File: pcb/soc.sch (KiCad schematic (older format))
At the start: 21 parts, among them IC5 CC2541F128RHAT, J1 CC Debugger, SW1 SW_Push, Y1 32 Mhz

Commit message: Added some documentation + TODO's
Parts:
- added C?: 1μF, symbol C_Small
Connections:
- net Earth: now also IC5.41 (GND(2)), C?.1
- net PIR_HIGH: now also IC5.9 (P1_1)
- net PIR_LOW: now also IC5.11 (P1_0)
- net at IC5.40 (DCOUPL): now also C?.2
- no-connect marks 2 -> 10
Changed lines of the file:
@@
 Comment4 ""
 $EndDescr
-Text HLabel 1200 4200 0    60   Input ~ 0
+Text HLabel 4050 3900 0    60   Input ~ 0
 PIR_HIGH
-Text HLabel 1200 4500 0    60   Input ~ 0
+Text HLabel 4500 4900 0    60   Input ~ 0
 PIR_LOW
 $Comp
@@
 L VCC #PWR22
 U 1 1 5A76E05D
-P 3850 3950
-F 0 "#PWR22" H 3850 3800 50  0001 C CNN
-F 1 "VCC" H 3850 4100 50  0000 C CNN
-F 2 "" H 3850 3950 50  0001 C CNN
-F 3 "" H 3850 3950 50  0001 C CNN
-	1    3850 3950
+P 3850 4250
+F 0 "#PWR22" H 3850 4100 50  0001 C CNN
+F 1 "VCC" H 3850 4400 50  0000 C CNN
+F 2 "" H 3850 4250 50  0001 C CNN
+F 3 "" H 3850 4250 50  0001 C CNN
+	1    3850 4250
 	1    0    0    -1
 $EndComp
@@
 Connection ~ 5950 3700
 Wire Wire Line
-	4250 4000 3850 4000
-Wire Wire Line
-	3850 4000 3850 3950
+	4250 4000 4100 4000
+Wire Wire Line
+	4100 4000 4100 4300
+Wire Wire Line
+	4100 4300 3850 4300
+Wire Wire Line
+	3850 4300 3850 4250
 Wire Wire Line
 	5550 1900 5550 1750
@@
 	1050 2550 1050 2400
 Wire Wire Line
-	1050 2000 1050 1850
+	1050 1850 1050 2000
 Wire Wire Line
 	1050 1550 1050 1400
@@
 Text Notes 2700 6300 2    60   ~ 0
 Debugger interface
+NoConn ~ 5350 4800
+NoConn ~ 5250 4800
+NoConn ~ 5150 4800
+NoConn ~ 5050 4800
+NoConn ~ 4950 4800
+NoConn ~ 4850 4800
+NoConn ~ 4750 4800
+NoConn ~ 4650 4800
+$Comp
+L Earth #PWR?
+U 1 1 5A76FB36
+P 4250 1900
+F 0 "#PWR?" H 4250 1650 50  0001 C CNN
+F 1 "Earth" H 4250 1750 50  0001 C CNN
+F 2 "" H 4250 1900 50  0001 C CNN
+F 3 "" H 4250 1900 50  0001 C CNN
+	1    4250 1900
+	1    0    0    -1
+$EndComp
+Wire Wire Line
+	4550 1900 4550 1800
+Wire Wire Line
+	4550 1800 4250 1800
+Wire Wire Line
+	4250 1800 4250 1900
+$Comp
+L C_Small C?
+U 1 1 5A770125
+P 4000 1650
+F 0 "C?" H 4010 1720 50  0000 L CNN
+F 1 "1μF" H 4010 1570 50  0000 L CNN
+F 2 "" H 4000 1650 50  0001 C CNN
+F 3 "" H 4000 1650 50  0001 C CNN
+	1    4000 1650
+	-1   0    0    1
+$EndComp
+$Comp
+L Earth #PWR?
+U 1 1 5A7703A1
+P 4000 1900
+F 0 "#PWR?" H 4000 1650 50  0001 C CNN
+F 1 "Earth" H 4000 1750 50  0001 C CNN
+F 2 "" H 4000 1900 50  0001 C CNN
+F 3 "" H 4000 1900 50  0001 C CNN
+	1    4000 1900
+	1    0    0    -1
+$EndComp
+Wire Wire Line
+	4650 1900 4650 1450
+Wire Wire Line
+	4000 1450 4000 1550
+Wire Wire Line
+	4000 1750 4000 1900
+Wire Wire Line
+	4650 1450 4000 1450
+Wire Wire Line
+	4250 3900 4050 3900
+Wire Wire Line
+	4500 4900 4550 4900
+Wire Wire Line
+	4550 4900 4550 4800
 $EndSCHEMATC

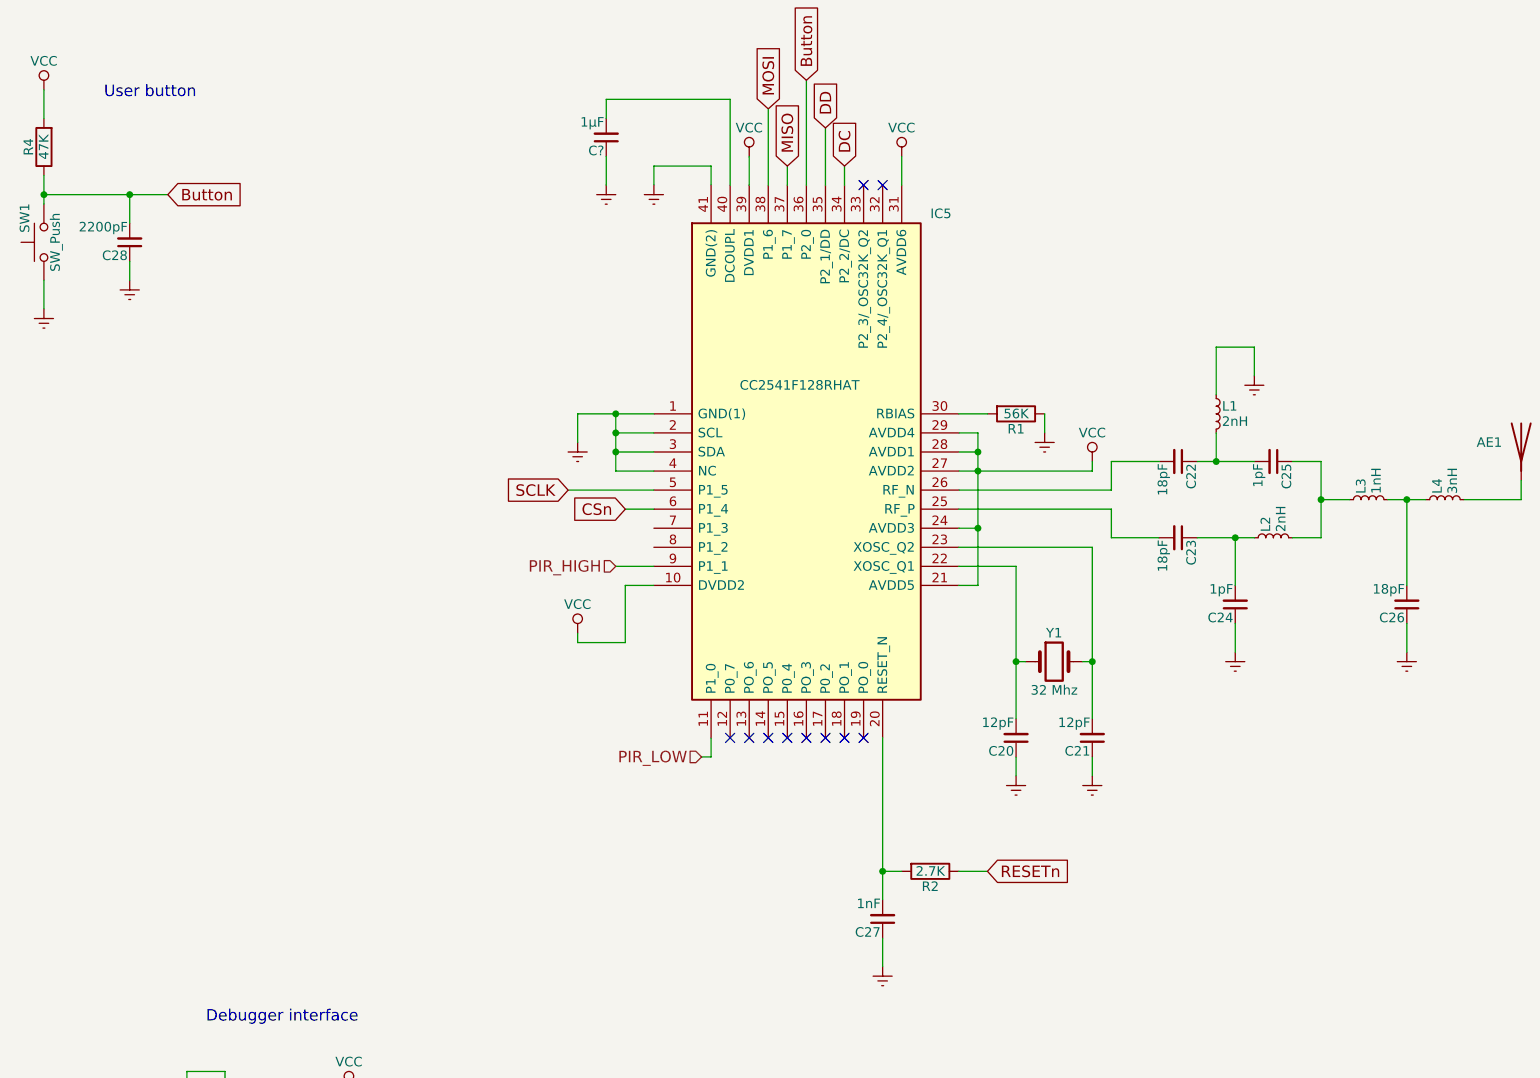
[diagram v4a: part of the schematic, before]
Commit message: Added light sensor with IIC interface
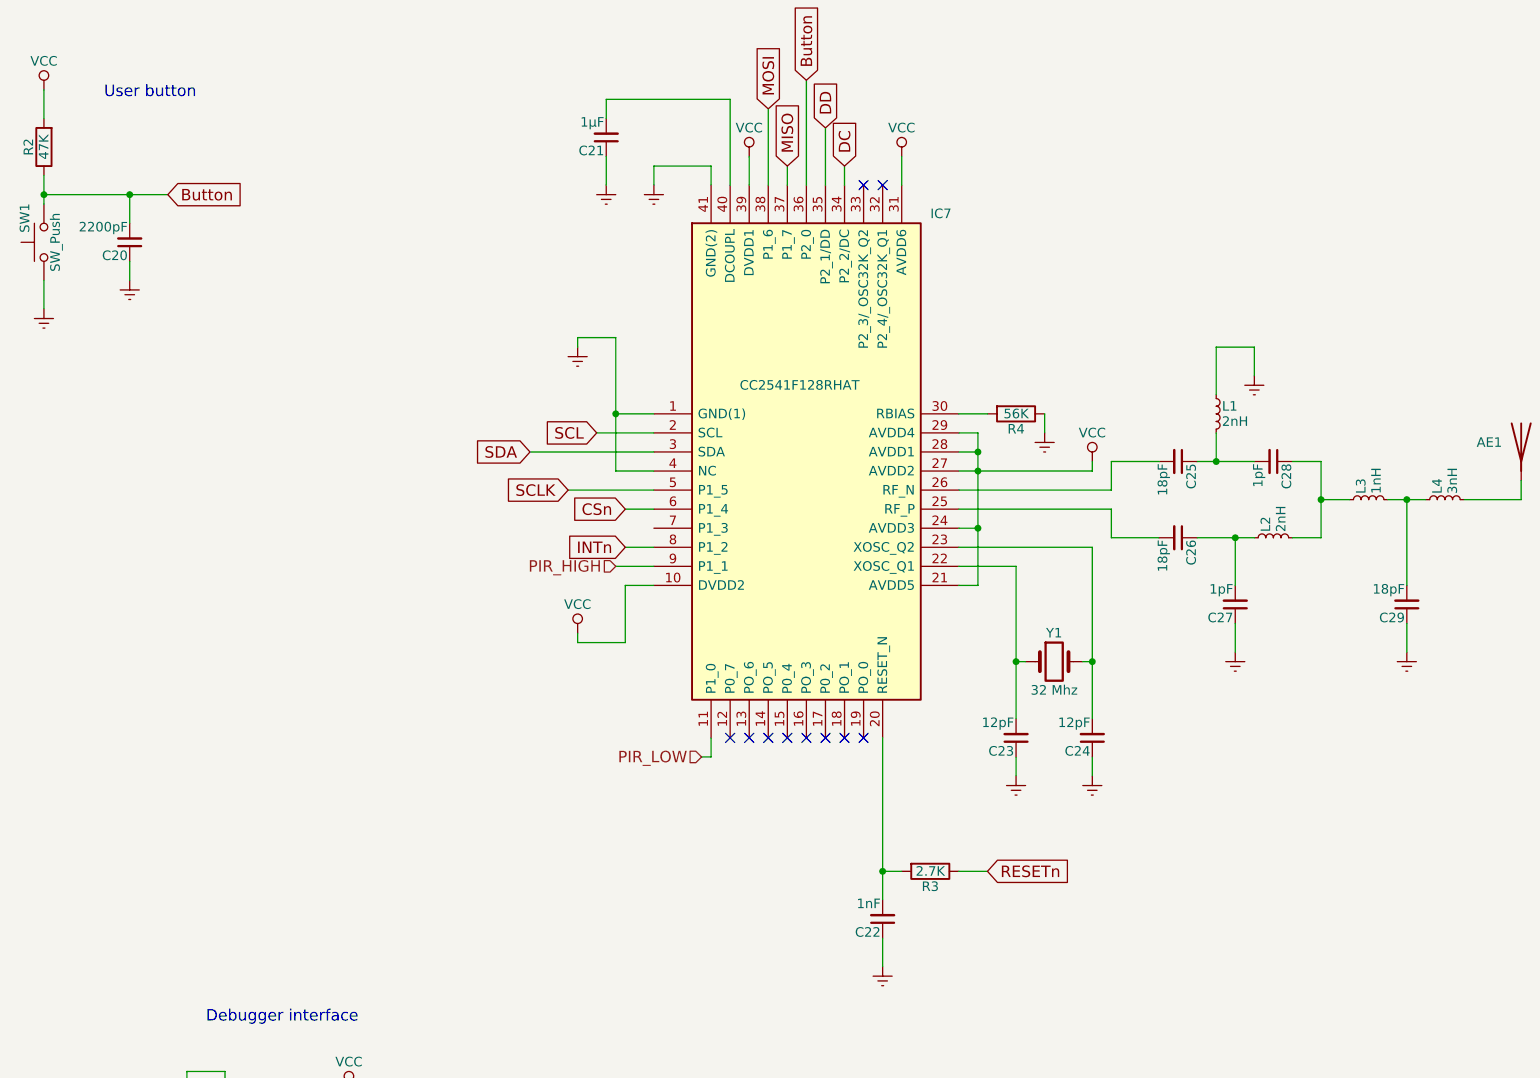
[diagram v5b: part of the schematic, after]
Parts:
- gave numbers to parts that had none: 1
- renumbered C28 to C20, C27 to C22, C20 to C23, C21 to C24, C22 to C25, C23 to C26, C24 to C27, C25 to C28, C26 to C29, IC5 to IC7, R4 to R2, R2 to R3, R1 to R4
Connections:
- net Earth: no longer IC7.2 (SCL), IC7.3 (SDA)
- net INTn: now reaches IC7.8 (P1_2)
- new net SCL: IC7.2 (SCL)
- new net SDA: IC7.3 (SDA)
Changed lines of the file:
@@
 LIBS:CC2541F256RHAR
 LIBS:CC2541F128RHAT
+LIBS:MAX44009EDT+T
 LIBS:pir-cache
 EELAYER 25 0
@@
 PIR_LOW
 $Comp
-L CC2541F128RHAT IC5
+L CC2541F128RHAT IC7
 U 1 1 5A76B408
 P 4250 3100
-F 0 "IC5" H 5700 4150 50  0000 L CNN
+F 0 "IC7" H 5700 4150 50  0000 L CNN
 F 1 "CC2541F128RHAT" H 4700 3250 50  0000 L CNN
 F 2 "QFN50P600X600X100-41N" H 5700 1450 50  0001 L CNN
@@
 SHUTTER
 $Comp
-L Earth #PWR21
+L Earth #PWR24
 U 1 1 5A76DE63
-P 3850 3250
-F 0 "#PWR21" H 3850 3000 50  0001 C CNN
-F 1 "Earth" H 3850 3100 50  0001 C CNN
-F 2 "" H 3850 3250 50  0001 C CNN
-F 3 "" H 3850 3250 50  0001 C CNN
-	1    3850 3250
-	1    0    0    -1
-$EndComp
-$Comp
-L VCC #PWR28
+P 3850 2750
+F 0 "#PWR24" H 3850 2500 50  0001 C CNN
+F 1 "Earth" H 3850 2600 50  0001 C CNN
+F 2 "" H 3850 2750 50  0001 C CNN
+F 3 "" H 3850 2750 50  0001 C CNN
+	1    3850 2750
+	1    0    0    -1
+$EndComp
+$Comp
+L VCC #PWR33
 U 1 1 5A76DE98
 P 6550 3350
-F 0 "#PWR28" H 6550 3200 50  0001 C CNN
+F 0 "#PWR33" H 6550 3200 50  0001 C CNN
 F 1 "VCC" H 6550 3500 50  0000 C CNN
 F 2 "" H 6550 3350 50  0001 C CNN
@@
 $EndComp
 $Comp
-L VCC #PWR22
+L VCC #PWR25
 U 1 1 5A76E05D
 P 3850 4250
-F 0 "#PWR22" H 3850 4100 50  0001 C CNN
+F 0 "#PWR25" H 3850 4100 50  0001 C CNN
 F 1 "VCC" H 3850 4400 50  0000 C CNN
 F 2 "" H 3850 4250 50  0001 C CNN
@@
 $EndComp
 $Comp
-L VCC #PWR25
+L VCC #PWR30
 U 1 1 5A76E1D1
 P 5550 1750
-F 0 "#PWR25" H 5550 1600 50  0001 C CNN
+F 0 "#PWR30" H 5550 1600 50  0001 C CNN
 F 1 "VCC" H 5550 1900 50  0000 C CNN
 F 2 "" H 5550 1750 50  0001 C CNN
@@
 $EndComp
 $Comp
-L VCC #PWR23
+L VCC #PWR28
 U 1 1 5A76E1F7
 P 4750 1750
-F 0 "#PWR23" H 4750 1600 50  0001 C CNN
+F 0 "#PWR28" H 4750 1600 50  0001 C CNN
 F 1 "VCC" H 4750 1900 50  0000 C CNN
 F 2 "" H 4750 1750 50  0001 C CNN
@@
 NoConn ~ 5350 1900
 $Comp
-L R R1
+L R R4
 U 1 1 5A76E4F0
 P 6150 3100
-F 0 "R1" V 6230 3100 50  0000 C CNN
+F 0 "R4" V 6230 3100 50  0000 C CNN
 F 1 "56K" V 6150 3100 50  0000 C CNN
 F 2 "" V 6080 3100 50  0001 C CNN
@@
 $EndComp
 $Comp
-L C_Small C22
+L C_Small C25
 U 1 1 5A76E83A
 P 7000 3350
-F 0 "C22" H 7010 3420 50  0000 L CNN
+F 0 "C25" H 7010 3420 50  0000 L CNN
 F 1 "18pF" H 7010 3270 50  0000 L CNN
 F 2 "" H 7000 3350 50  0001 C CNN
@@
 $EndComp
 $Comp
-L C_Small C23
+L C_Small C26
 U 1 1 5A76EB9B
 P 7000 3750
-F 0 "C23" H 7010 3820 50  0000 L CNN
+F 0 "C26" H 7010 3820 50  0000 L CNN
 F 1 "18pF" H 7010 3670 50  0000 L CNN
 F 2 "" H 7000 3750 50  0001 C CNN
@@
 $EndComp
 $Comp
-L C_Small C25
+L C_Small C28
 U 1 1 5A76EBCB
 P 7500 3350
-F 0 "C25" H 7510 3420 50  0000 L CNN
+F 0 "C28" H 7510 3420 50  0000 L CNN
 F 1 "1pF" H 7510 3270 50  0000 L CNN
 F 2 "" H 7500 3350 50  0001 C CNN
@@
 $EndComp
 $Comp
-L C_Small C24
+L C_Small C27
 U 1 1 5A76EC10
 P 7300 4100
-F 0 "C24" H 7310 4170 50  0000 L CNN
+F 0 "C27" H 7310 4170 50  0000 L CNN
 F 1 "1pF" H 7310 4020 50  0000 L CNN
 F 2 "" H 7300 4100 50  0001 C CNN
@@
 $EndComp
 $Comp
-L Earth #PWR30
+L Earth #PWR35
 U 1 1 5A76EF79
 P 7300 4350
-F 0 "#PWR30" H 7300 4100 50  0001 C CNN
+F 0 "#PWR35" H 7300 4100 50  0001 C CNN
 F 1 "Earth" H 7300 4200 50  0001 C CNN
 F 2 "" H 7300 4350 50  0001 C CNN
@@
 $EndComp
 $Comp
-L Earth #PWR27
+L Earth #PWR32
 U 1 1 5A76F127
 P 6300 3200
-F 0 "#PWR27" H 6300 2950 50  0001 C CNN
+F 0 "#PWR32" H 6300 2950 50  0001 C CNN
 F 1 "Earth" H 6300 3050 50  0001 C CNN
 F 2 "" H 6300 3200 50  0001 C CNN
@@
 $EndComp
 $Comp
-L Earth #PWR31
+L Earth #PWR36
 U 1 1 5A76F249
 P 7400 2900
-F 0 "#PWR31" H 7400 2650 50  0001 C CNN
+F 0 "#PWR36" H 7400 2650 50  0001 C CNN
 F 1 "Earth" H 7400 2750 50  0001 C CNN
 F 2 "" H 7400 2900 50  0001 C CNN
@@
 $EndComp
 $Comp
-L C_Small C26
+L C_Small C29
 U 1 1 5A76F398
 P 8200 4100
-F 0 "C26" H 8210 4170 50  0000 L CNN
+F 0 "C29" H 8210 4170 50  0000 L CNN
 F 1 "18pF" H 8210 4020 50  0000 L CNN
 F 2 "" H 8200 4100 50  0001 C CNN
@@
 $EndComp
 $Comp
-L Earth #PWR32
+L Earth #PWR37
 U 1 1 5A76F405
 P 8200 4350
-F 0 "#PWR32" H 8200 4100 50  0001 C CNN
+F 0 "#PWR37" H 8200 4100 50  0001 C CNN
 F 1 "Earth" H 8200 4200 50  0001 C CNN
 F 2 "" H 8200 4350 50  0001 C CNN
@@
 $EndComp
 $Comp
-L C_Small C20
+L C_Small C23
 U 1 1 5A76F951
 P 6150 4800
-F 0 "C20" H 6160 4870 50  0000 L CNN
+F 0 "C23" H 6160 4870 50  0000 L CNN
 F 1 "12pF" H 6160 4720 50  0000 L CNN
 F 2 "" H 6150 4800 50  0001 C CNN
@@
 $EndComp
 $Comp
-L C_Small C21
+L C_Small C24
 U 1 1 5A76F9C8
 P 6550 4800
-F 0 "C21" H 6560 4870 50  0000 L CNN
+F 0 "C24" H 6560 4870 50  0000 L CNN
 F 1 "12pF" H 6560 4720 50  0000 L CNN
 F 2 "" H 6550 4800 50  0001 C CNN
@@
 $EndComp
 Wire Wire Line
-	3850 3100 4250 3100
-Wire Wire Line
-	3850 3100 3850 3250
-Wire Wire Line
-	4250 3200 4050 3200
-Wire Wire Line
-	4050 3100 4050 3400
+	3850 2700 4050 2700
+Wire Wire Line
+	4050 2700 4050 3400
+Wire Wire Line
+	4050 3100 4250 3100
+Wire Wire Line
+	3850 2700 3850 2750
 Connection ~ 4050 3100
 Wire Wire Line
-	4050 3300 4250 3300
-Connection ~ 4050 3200
-Wire Wire Line
 	4050 3400 4250 3400
-Connection ~ 4050 3300
 Wire Wire Line
 	5850 3400 6550 3400
@@
 Connection ~ 6550 4400
 $Comp
-L Earth #PWR26
+L Earth #PWR31
 U 1 1 5A76FDE5
 P 6150 5000
-F 0 "#PWR26" H 6150 4750 50  0001 C CNN
+F 0 "#PWR31" H 6150 4750 50  0001 C CNN
 F 1 "Earth" H 6150 4850 50  0001 C CNN
 F 2 "" H 6150 5000 50  0001 C CNN
@@
 $EndComp
 $Comp
-L Earth #PWR29
+L Earth #PWR34
 U 1 1 5A76FE1D
 P 6550 5000
-F 0 "#PWR29" H 6550 4750 50  0001 C CNN
+F 0 "#PWR34" H 6550 4750 50  0001 C CNN
 F 1 "Earth" H 6550 4850 50  0001 C CNN
 F 2 "" H 6550 5000 50  0001 C CNN
@@
 	1900 6900 2050 6900
 $Comp
-L Earth #PWR18
+L Earth #PWR22
 U 1 1 5A762D06
 P 1800 6650
-F 0 "#PWR18" H 1800 6400 50  0001 C CNN
+F 0 "#PWR22" H 1800 6400 50  0001 C CNN
 F 1 "Earth" H 1800 6500 50  0001 C CNN
 F 2 "" H 1800 6650 50  0001 C CNN
@@
 	1800 6550 1800 6650
 $Comp
-L VCC #PWR20
+L VCC #PWR23
 U 1 1 5A762F97
 P 2650 6650
-F 0 "#PWR20" H 2650 6500 50  0001 C CNN
+F 0 "#PWR23" H 2650 6500 50  0001 C CNN
 F 1 "VCC" H 2650 6800 50  0000 C CNN
 F 2 "" H 2650 6650 50  0001 C CNN
@@
 	4950 1800 4950 1900
 $Comp
-L R R2
+L R R3
 U 1 1 5A7649A0
 P 5700 5500
-F 0 "R2" V 5780 5500 50  0000 C CNN
+F 0 "R3" V 5780 5500 50  0000 C CNN
 F 1 "2.7K" V 5700 5500 50  0000 C CNN
 F 2 "" V 5630 5500 50  0001 C CNN
@@
 	6000 5500 5850 5500
 $Comp
-L C_Small C27
+L C_Small C22
 U 1 1 5A764EFF
 P 5450 5750
-F 0 "C27" H 5460 5820 50  0000 L CNN
+F 0 "C22" H 5460 5820 50  0000 L CNN
 F 1 "1nF" H 5460 5670 50  0000 L CNN
 F 2 "" H 5450 5750 50  0001 C CNN
@@
 $EndComp
 $Comp
-L Earth #PWR24
+L Earth #PWR29
 U 1 1 5A764F83
 P 5450 6000
-F 0 "#PWR24" H 5450 5750 50  0001 C CNN
+F 0 "#PWR29" H 5450 5750 50  0001 C CNN
 F 1 "Earth" H 5450 5850 50  0001 C CNN
 F 2 "" H 5450 6000 50  0001 C CNN
@@
 CC3V3
 $Comp
-L VCC #PWR16
+L VCC #PWR19
 U 1 1 5A76CA51
 P 1050 1400
-F 0 "#PWR16" H 1050 1250 50  0001 C CNN
+F 0 "#PWR19" H 1050 1250 50  0001 C CNN
 F 1 "VCC" H 1050 1550 50  0000 C CNN
 F 2 "" H 1050 1400 50  0001 C CNN
@@
 $EndComp
 $Comp
-L R R4
+L R R2
 U 1 1 5A76CB17
 P 1050 1700
-F 0 "R4" V 1130 1700 50  0000 C CNN
+F 0 "R2" V 1130 1700 50  0000 C CNN
 F 1 "47K" V 1050 1700 50  0000 C CNN
 F 2 "" V 980 1700 50  0001 C CNN
@@
 $EndComp
 $Comp
-L C_Small C28
+L C_Small C20
 U 1 1 5A76CF70
 P 1500 2200
-F 0 "C28" H 1510 2270 50  0000 L CNN
+F 0 "C20" H 1510 2270 50  0000 L CNN
 F 1 "2200pF" H 1510 2120 50  0000 L CNN
 F 2 "" H 1500 2200 50  0001 C CNN
@@
 $EndComp
 $Comp
-L Earth #PWR17
+L Earth #PWR20
 U 1 1 5A76D398
 P 1050 2550
-F 0 "#PWR17" H 1050 2300 50  0001 C CNN
+F 0 "#PWR20" H 1050 2300 50  0001 C CNN
 F 1 "Earth" H 1050 2400 50  0001 C CNN
 F 2 "" H 1050 2550 50  0001 C CNN
@@
 Connection ~ 1050 1950
 $Comp
-L Earth #PWR19
+L Earth #PWR21
 U 1 1 5A76D8AA
 P 1500 2400
-F 0 "#PWR19" H 1500 2150 50  0001 C CNN
+F 0 "#PWR21" H 1500 2150 50  0001 C CNN
 F 1 "Earth" H 1500 2250 50  0001 C CNN
 F 2 "" H 1500 2400 50  0001 C CNN
@@
 NoConn ~ 4650 4800
 $Comp
-L Earth #PWR?
+L Earth #PWR27
 U 1 1 5A76FB36
 P 4250 1900
-F 0 "#PWR?" H 4250 1650 50  0001 C CNN
+F 0 "#PWR27" H 4250 1650 50  0001 C CNN
 F 1 "Earth" H 4250 1750 50  0001 C CNN
 F 2 "" H 4250 1900 50  0001 C CNN
@@
 	4250 1800 4250 1900
 $Comp
-L C_Small C?
+L C_Small C21
 U 1 1 5A770125
 P 4000 1650
-F 0 "C?" H 4010 1720 50  0000 L CNN
+F 0 "C21" H 4010 1720 50  0000 L CNN
 F 1 "1μF" H 4010 1570 50  0000 L CNN
 F 2 "" H 4000 1650 50  0001 C CNN
@@
 $EndComp
 $Comp
-L Earth #PWR?
+L Earth #PWR26
 U 1 1 5A7703A1
 P 4000 1900
-F 0 "#PWR?" H 4000 1650 50  0001 C CNN
+F 0 "#PWR26" H 4000 1650 50  0001 C CNN
 F 1 "Earth" H 4000 1750 50  0001 C CNN
 F 2 "" H 4000 1900 50  0001 C CNN
@@
 Wire Wire Line
 	4550 4900 4550 4800
+Text GLabel 3950 3200 0    60   Input ~ 0
+SCL
+Text GLabel 3600 3300 0    60   Input ~ 0
+SDA
+Wire Wire Line
+	3950 3200 4250 3200
+Wire Wire Line
+	4250 3300 3600 3300
+Text GLabel 4100 3800 0    60   Input ~ 0
+INTn
+Wire Wire Line
+	4250 3800 4100 3800
 $EndSCHEMATC
